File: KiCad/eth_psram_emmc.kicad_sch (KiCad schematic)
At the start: 39 parts, among them IC5 MX52LM04A11XVW, IC6 LAN8742A-CZ-TR, IC7 APS256XXN-OBR-BG, Y2 VXM7-9032-25M0000000

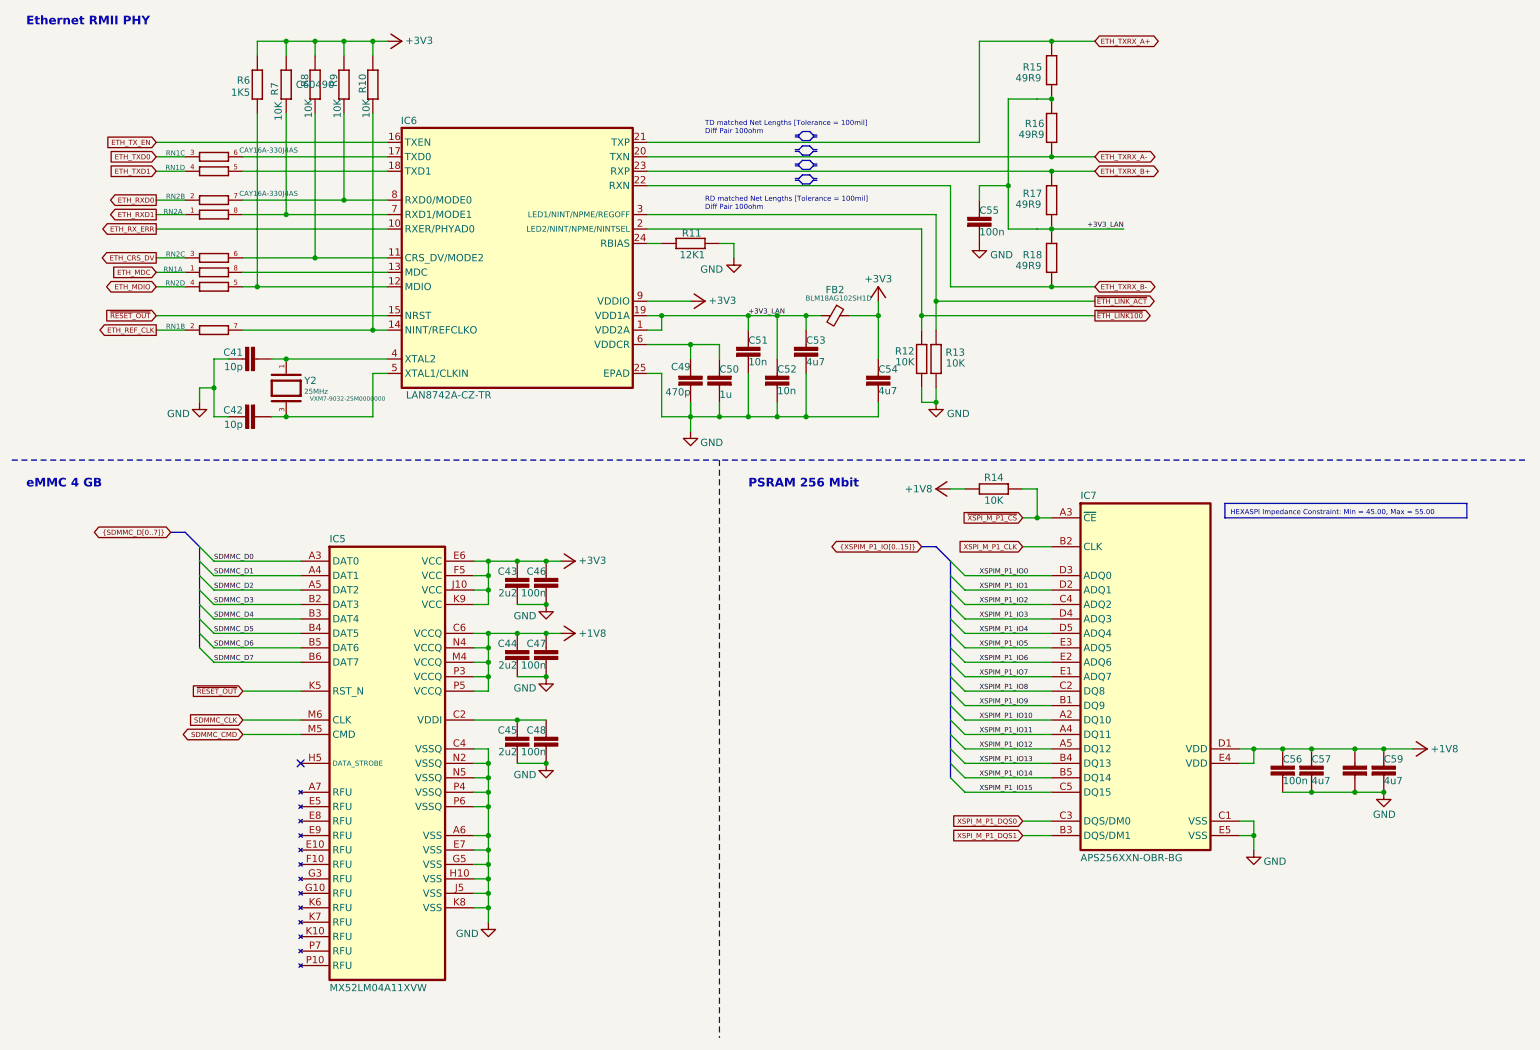
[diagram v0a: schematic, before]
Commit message: Folders paths adjusted, Cin added to 3V3 LDO
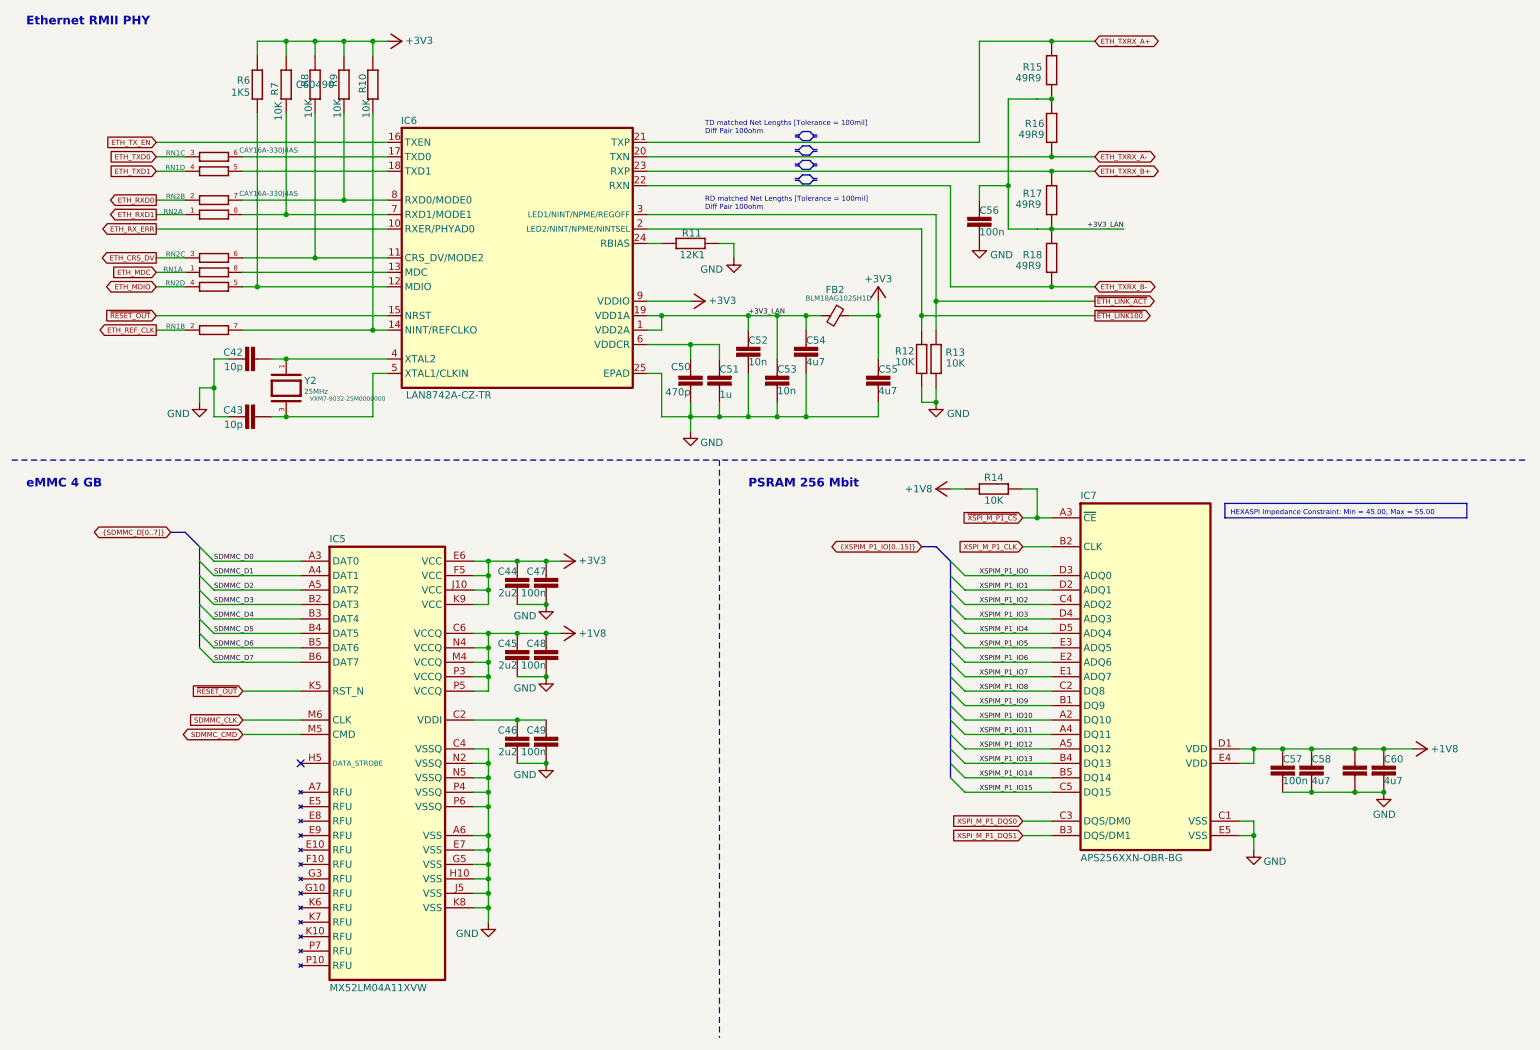
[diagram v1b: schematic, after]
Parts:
- renumbered C41 to C42, C42 to C43, C43 to C44, C44 to C45, C45 to C46, C46 to C47, C47 to C48, C48 to C49, C49 to C50, C50 to C51, C51 to C52, C52 to C53, C53 to C54, C54 to C55, C55 to C56, C56 to C57, C57 to C58, C58 to C59, C59 to C60
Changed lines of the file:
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@@
 	(title_block
 		(title "${project_name}")
-		(date "2025-11-02")
+		(date "2025-11-03")
 		(rev "${project_version}")
 		(company "${project_creator}")
@@
 	)
 	(junction
+		(at 198.12 43.18)
+		(diameter 0)
+		(color 0 0 0 0)
+	)
+	(junction
 		(at 73.66 48.26)
 		(diameter 0)
@@
 	)
 	(junction
-		(at 198.12 43.18)
-		(diameter 0)
-		(color 0 0 0 0)
-	)
-	(junction
 		(at 99.06 129.54)
 		(diameter 0)
@@
 	(wire
 		(pts
-			(xy 127 45.72) (xy 180.34 45.72)
-		)
-		(stroke
-			(width 0.1524)
-			(type solid)
-		)
-	)
-	(wire
-		(pts
 			(xy 127 50.8) (xy 177.8 50.8)
 		)
@@
 	(wire
 		(pts
+			(xy 127 45.72) (xy 180.34 45.72)
+		)
+		(stroke
+			(width 0)
+			(type default)
+		)
+	)
+	(wire
+		(pts
 			(xy 96.52 147.32) (xy 99.06 147.32)
 		)
@@
 	(wire
 		(pts
+			(xy 127 43.18) (xy 198.12 43.18)
+		)
+		(stroke
+			(width 0)
+			(type default)
+		)
+	)
+	(wire
+		(pts
 			(xy 233.68 157.48) (xy 233.68 160.02)
 		)
@@
 	(wire
 		(pts
-			(xy 127 43.18) (xy 198.12 43.18)
-		)
-		(stroke
-			(width 0.1524)
-			(type solid)
-		)
-	)
-	(wire
-		(pts
 			(xy 198.12 30.48) (xy 195.58 30.48)
 		)
@@
 		(on_board yes)
 		(dnp no)
-		(property "Reference" "C52"
+		(property "Reference" "C53"
 			(at 149.86 78.74 0)
 			(effects
@@
 			(project "BB3plus CM5 STM32H7 module"
 				(path "/1a4f0aea-3a69-423f-8790-3103cd0321c4/db533ab3-e8cc-4dba-934e-bd27ee1dfc29"
-					(reference "C52")
+					(reference "C53")
 					(unit 1)
 				)
@@
 		(on_board yes)
 		(dnp no)
-		(property "Reference" "C51"
+		(property "Reference" "C52"
 			(at 144.78 73.66 0)
 			(effects
@@
 			(project "BB3plus CM5 STM32H7 module"
 				(path "/1a4f0aea-3a69-423f-8790-3103cd0321c4/db533ab3-e8cc-4dba-934e-bd27ee1dfc29"
-					(reference "C51")
+					(reference "C52")
 					(unit 1)
 				)
@@
 		(on_board yes)
 		(dnp no)
-		(property "Reference" "C59"
+		(property "Reference" "C60"
 			(at 256.54 147.32 0)
 			(effects
@@
 			(project "BB3plus CM5 STM32H7 module"
 				(path "/1a4f0aea-3a69-423f-8790-3103cd0321c4/db533ab3-e8cc-4dba-934e-bd27ee1dfc29"
-					(reference "C59")
+					(reference "C60")
 					(unit 1)
 				)
@@
 		(on_board yes)
 		(dnp no)
-		(property "Reference" "C47"
+		(property "Reference" "C48"
 			(at 109.22 127 0)
 			(effects
@@
 			(project "BB3plus CM5 STM32H7 module"
 				(path "/1a4f0aea-3a69-423f-8790-3103cd0321c4/db533ab3-e8cc-4dba-934e-bd27ee1dfc29"
-					(reference "C47")
+					(reference "C48")
 					(unit 1)
 				)
@@
 		(on_board yes)
 		(dnp no)
-		(property "Reference" "C44"
+		(property "Reference" "C45"
 			(at 104.14 127 0)
 			(effects
@@
 			(project "BB3plus CM5 STM32H7 module"
 				(path "/1a4f0aea-3a69-423f-8790-3103cd0321c4/db533ab3-e8cc-4dba-934e-bd27ee1dfc29"
-					(reference "C44")
+					(reference "C45")
 					(unit 1)
 				)
@@
 		(on_board yes)
 		(dnp no)
-		(property "Reference" "C56"
+		(property "Reference" "C57"
 			(at 238.76 147.32 0)
 			(effects
@@
 			(project "BB3plus CM5 STM32H7 module"
 				(path "/1a4f0aea-3a69-423f-8790-3103cd0321c4/db533ab3-e8cc-4dba-934e-bd27ee1dfc29"
-					(reference "C56")
+					(reference "C57")
 					(unit 1)
 				)
@@
 		(on_board yes)
 		(dnp no)
-		(property "Reference" "C55"
+		(property "Reference" "C56"
 			(at 185.42 50.8 0)
 			(effects
@@
 			(project "BB3plus CM5 STM32H7 module"
 				(path "/1a4f0aea-3a69-423f-8790-3103cd0321c4/db533ab3-e8cc-4dba-934e-bd27ee1dfc29"
-					(reference "C55")
+					(reference "C56")
 					(unit 1)
 				)
@@
 		(on_board yes)
 		(dnp no)
-		(property "Reference" "C53"
+		(property "Reference" "C54"
 			(at 154.94 73.66 0)
 			(effects
@@
 			(project "BB3plus CM5 STM32H7 module"
 				(path "/1a4f0aea-3a69-423f-8790-3103cd0321c4/db533ab3-e8cc-4dba-934e-bd27ee1dfc29"
-					(reference "C53")
+					(reference "C54")
 					(unit 1)
 				)
@@
 		(on_board yes)
 		(dnp no)
-		(property "Reference" "#PWR014"
+		(property "Reference" "#PWR015"
 			(at 260.35 144.78 0)
 			(effects
@@
 			(project "BB3plus CM5 STM32H7 module"
 				(path "/1a4f0aea-3a69-423f-8790-3103cd0321c4/db533ab3-e8cc-4dba-934e-bd27ee1dfc29"
-					(reference "#PWR014")
+					(reference "#PWR015")
 					(unit 1)
 				)
@@
 		(on_board yes)
 		(dnp no)
-		(property "Reference" "C50"
+		(property "Reference" "C51"
 			(at 139.7 78.74 0)
 			(effects
@@
 			(project "BB3plus CM5 STM32H7 module"
 				(path "/1a4f0aea-3a69-423f-8790-3103cd0321c4/db533ab3-e8cc-4dba-934e-bd27ee1dfc29"
-					(reference "C50")
+					(reference "C51")
 					(unit 1)
 				)
@@
 		(on_board yes)
 		(dnp no)
-		(property "Reference" "#PWR013"
+		(property "Reference" "#PWR014"
 			(at 181.61 99.06 0)
 			(effects
@@
 			(project "BB3plus CM5 STM32H7 module"
 				(path "/1a4f0aea-3a69-423f-8790-3103cd0321c4/db533ab3-e8cc-4dba-934e-bd27ee1dfc29"
-					(reference "#PWR013")
+					(reference "#PWR014")
 					(unit 1)
 				)
@@
 		(on_board yes)
 		(dnp no)
-		(property "Reference" "#PWR012"
+		(property "Reference" "#PWR013"
 			(at 110.49 124.46 0)
 			(effects
@@
 			(project "BB3plus CM5 STM32H7 module"
 				(path "/1a4f0aea-3a69-423f-8790-3103cd0321c4/db533ab3-e8cc-4dba-934e-bd27ee1dfc29"
-					(reference "#PWR012")
+					(reference "#PWR013")
 					(unit 1)
 				)
@@
 		(on_board yes)
 		(dnp no)
-		(property "Reference" "C45"
+		(property "Reference" "C46"
 			(at 104.14 142.24 0)
 			(effects
@@
 			(project "BB3plus CM5 STM32H7 module"
 				(path "/1a4f0aea-3a69-423f-8790-3103cd0321c4/db533ab3-e8cc-4dba-934e-bd27ee1dfc29"
-					(reference "C45")
+					(reference "C46")
 					(unit 1)
 				)
@@
 		(on_board yes)
 		(dnp no)
-		(property "Reference" "C48"
+		(property "Reference" "C49"
 			(at 109.22 142.24 0)
 			(effects
@@
 			(project "BB3plus CM5 STM32H7 module"
 				(path "/1a4f0aea-3a69-423f-8790-3103cd0321c4/db533ab3-e8cc-4dba-934e-bd27ee1dfc29"
-					(reference "C48")
+					(reference "C49")
 					(unit 1)
 				)
@@
 		(on_board yes)
 		(dnp no)
-		(property "Reference" "C46"
+		(property "Reference" "C47"
 			(at 109.22 114.3 0)
 			(effects
@@
 			(project "BB3plus CM5 STM32H7 module"
 				(path "/1a4f0aea-3a69-423f-8790-3103cd0321c4/db533ab3-e8cc-4dba-934e-bd27ee1dfc29"
-					(reference "C46")
+					(reference "C47")
 					(unit 1)
 				)
@@
 		(on_board yes)
 		(dnp no)
-		(property "Reference" "C49"
+		(property "Reference" "C50"
 			(at 134.62 76.835 0)
 			(effects
@@
 			(project "BB3plus CM5 STM32H7 module"
 				(path "/1a4f0aea-3a69-423f-8790-3103cd0321c4/db533ab3-e8cc-4dba-934e-bd27ee1dfc29"
-					(reference "C49")
+					(reference "C50")
 					(unit 1)
 				)
@@
 		(on_board yes)
 		(dnp no)
-		(property "Reference" "C57"
+		(property "Reference" "C58"
 			(at 243.84 147.32 0)
 			(effects
@@
 			(project "BB3plus CM5 STM32H7 module"
 				(path "/1a4f0aea-3a69-423f-8790-3103cd0321c4/db533ab3-e8cc-4dba-934e-bd27ee1dfc29"
-					(reference "C57")
+					(reference "C58")
 					(unit 1)
 				)
@@
 		(on_board yes)
 		(dnp no)
-		(property "Reference" "C41"
+		(property "Reference" "C42"
 			(at 55.88 74.295 90)
 			(effects
@@
 			(project "BB3plus CM5 STM32H7 module"
 				(path "/1a4f0aea-3a69-423f-8790-3103cd0321c4/db533ab3-e8cc-4dba-934e-bd27ee1dfc29"
-					(reference "C41")
+					(reference "C42")
 					(unit 1)
 				)
@@
 		(on_board yes)
 		(dnp no)
-		(property "Reference" "C42"
+		(property "Reference" "C43"
 			(at 55.88 84.455 90)
 			(effects
@@
 			(project "BB3plus CM5 STM32H7 module"
 				(path "/1a4f0aea-3a69-423f-8790-3103cd0321c4/db533ab3-e8cc-4dba-934e-bd27ee1dfc29"
-					(reference "C42")
+					(reference "C43")
 					(unit 1)
 				)
@@
 		(on_board yes)
 		(dnp no)
-		(property "Reference" "C54"
+		(property "Reference" "C55"
 			(at 167.64 78.74 0)
 			(effects
@@
 			(project "BB3plus CM5 STM32H7 module"
 				(path "/1a4f0aea-3a69-423f-8790-3103cd0321c4/db533ab3-e8cc-4dba-934e-bd27ee1dfc29"
-					(reference "C54")
+					(reference "C55")
 					(unit 1)
 				)
@@
 		(on_board yes)
 		(dnp no)
-		(property "Reference" "C58"
+		(property "Reference" "C59"
 			(at 251.46 147.32 0)
 			(effects
@@
 			(project "BB3plus CM5 STM32H7 module"
 				(path "/1a4f0aea-3a69-423f-8790-3103cd0321c4/db533ab3-e8cc-4dba-934e-bd27ee1dfc29"
-					(reference "C58")
+					(reference "C59")
 					(unit 1)
 				)
@@
 		(on_board yes)
 		(dnp no)
-		(property "Reference" "C43"
+		(property "Reference" "C44"
 			(at 104.14 114.3 0)
 			(effects
@@
 			(project "BB3plus CM5 STM32H7 module"
 				(path "/1a4f0aea-3a69-423f-8790-3103cd0321c4/db533ab3-e8cc-4dba-934e-bd27ee1dfc29"
-					(reference "C43")
+					(reference "C44")
 					(unit 1)
 				)

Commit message: BOM update
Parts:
- C54, C55, C58, C60: Mouser 187-CL10A475KP8NNNC -> 187-CL10A475KP8NNND
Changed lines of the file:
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@@
 			)
 		)
-		(property "Mouser" "187-CL10A475KP8NNNC"
+		(property "Mouser" "187-CL10A475KP8NNND"
 			(at 256.54 147.32 0)
 			(effects
@@
 			)
 		)
-		(property "Mouser" "187-CL10A475KP8NNNC"
+		(property "Mouser" "187-CL10A475KP8NNND"
 			(at 154.94 73.66 0)
 			(effects
@@
 		(dnp no)
 		(property "Reference" "R8"
-			(at 66.04 26.035 90)
+			(at 67.31 29.845 90)
 			(effects
 				(font
 					(size 1.27 1.27)
 				)
-				(justify right top)
+				(justify left bottom)
 			)
 		)
@@
 					(size 1.27 1.27)
 				)
+				(hide yes)
 			)
 		)
@@
 			)
 		)
-		(property "Mouser" "187-CL10A475KP8NNNC"
+		(property "Mouser" "187-CL10A475KP8NNND"
 			(at 243.84 147.32 0)
 			(effects
@@
 			)
 		)
-		(property "Mouser" "187-CL10A475KP8NNNC"
+		(property "Mouser" "187-CL10A475KP8NNND"
 			(at 167.64 78.74 0)
 			(effects
@@
 		(dnp no)
 		(property "Reference" "R9"
-			(at 71.12 26.035 90)
+			(at 72.39 29.845 90)
 			(effects
 				(font
 					(size 1.27 1.27)
 				)
-				(justify right top)
+				(justify left bottom)
 			)
 		)
@@
 		(dnp no)
 		(property "Reference" "R10"
-			(at 76.2 26.035 90)
+			(at 77.47 29.845 90)
 			(effects
 				(font
 					(size 1.27 1.27)
 				)
-				(justify right top)
+				(justify left bottom)
 			)
 		)
